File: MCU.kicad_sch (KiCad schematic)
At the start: 31 parts, among them J10 SWD, J11 UART, J12 I2C1, Q16 AO3401A, Q17 2N7002W, U12 STM32F030C8Tx

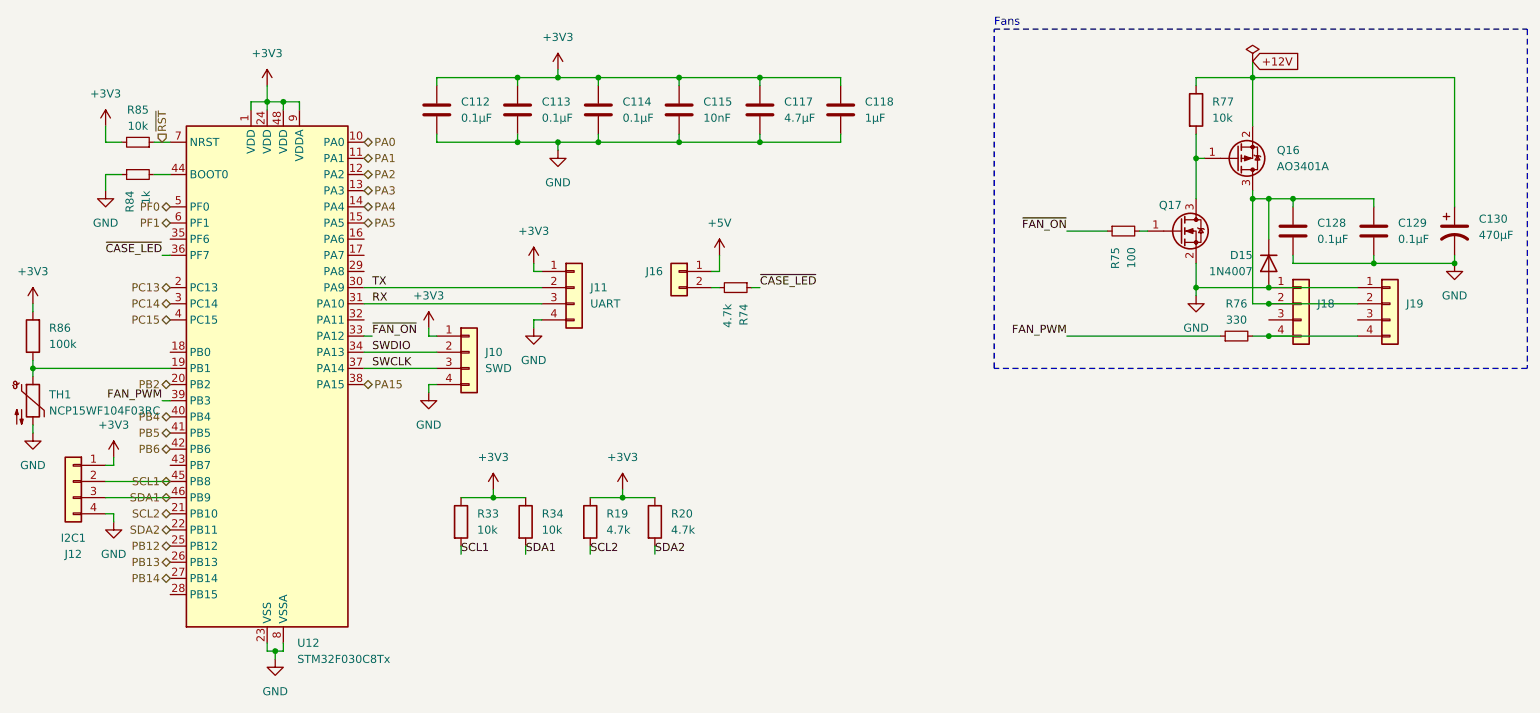
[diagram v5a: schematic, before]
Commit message: pcb: fixed fan capacitor and changed case led resistor value
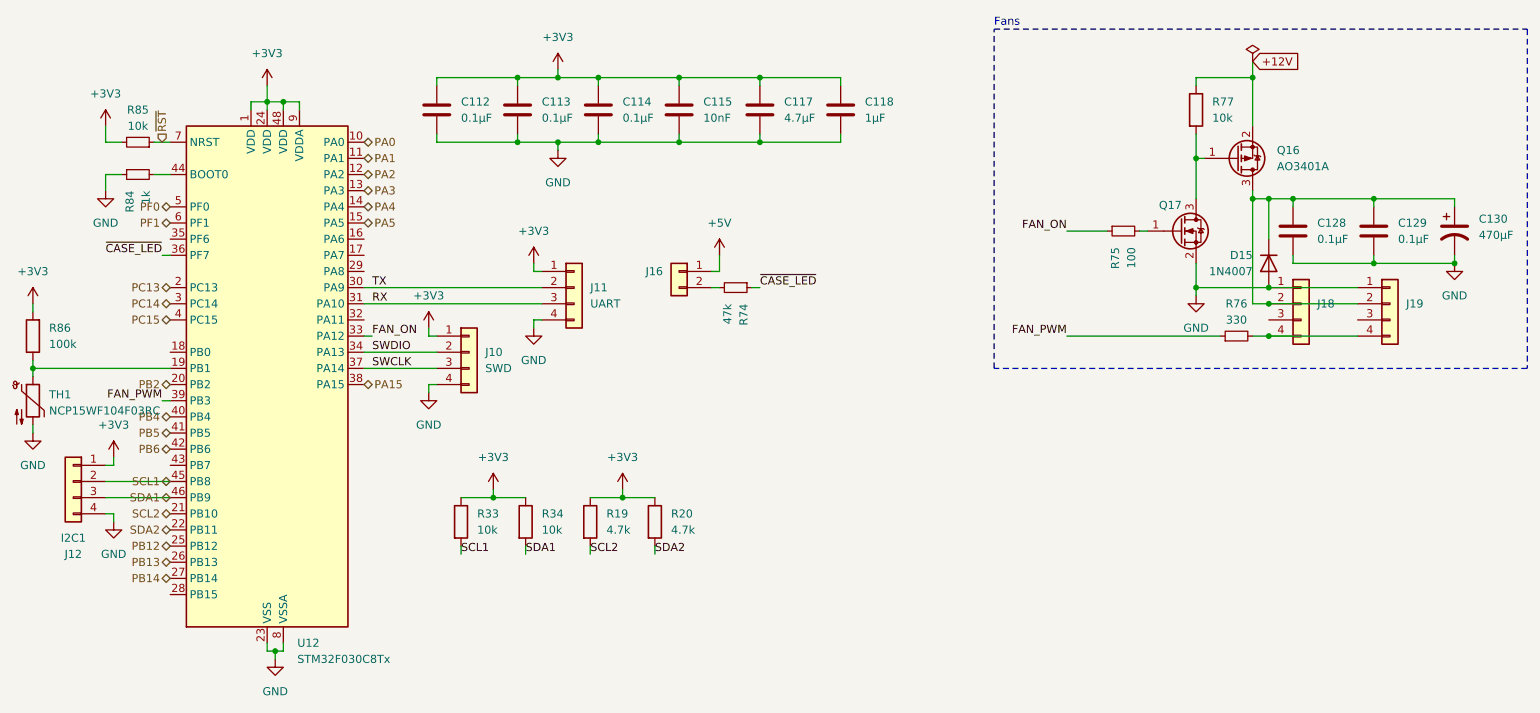
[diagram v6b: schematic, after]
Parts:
- R74: value 4.7k -> 47k; LCSC C25900 -> C25792; Part_Number 0402WGF4701TCE -> 0402WGF4702TCE
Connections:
- net +12V: no longer C130.1
- net at C128.1, C129.1, D15.1 (K)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: now also C130.1
- net ~{FAN_ON} renamed FAN_ON
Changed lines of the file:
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@@
 	)
 	(junction
+		(at 229.87 49.53)
+		(diameter 0)
+		(color 0 0 0 0)
+	)
+	(junction
 		(at 213.36 66.04)
 		(diameter 0)
@@
 	(wire
 		(pts
-			(xy 242.57 30.48) (xy 210.82 30.48)
+			(xy 30.48 45.72) (xy 30.48 48.26)
 		)
 		(stroke
@@
 	(wire
 		(pts
-			(xy 30.48 45.72) (xy 30.48 48.26)
+			(xy 229.87 49.53) (xy 229.87 50.8)
 		)
 		(stroke
@@
 	(wire
 		(pts
-			(xy 229.87 49.53) (xy 229.87 50.8)
+			(xy 86.36 104.14) (xy 86.36 105.41)
 		)
 		(stroke
@@
 	(wire
 		(pts
-			(xy 242.57 30.48) (xy 242.57 50.8)
+			(xy 95.25 30.48) (xy 101.6 30.48)
 		)
 		(stroke
@@
 	(wire
 		(pts
-			(xy 86.36 104.14) (xy 86.36 105.41)
+			(xy 30.48 91.44) (xy 31.75 91.44)
 		)
 		(stroke
@@
 	(wire
 		(pts
-			(xy 95.25 30.48) (xy 101.6 30.48)
+			(xy 120.65 40.64) (xy 120.65 39.37)
 		)
 		(stroke
@@
 	(wire
 		(pts
-			(xy 30.48 91.44) (xy 31.75 91.44)
+			(xy 127 63.5) (xy 125.73 63.5)
 		)
 		(stroke
@@
 	(wire
 		(pts
-			(xy 120.65 40.64) (xy 120.65 39.37)
+			(xy 71.12 71.12) (xy 72.39 71.12)
 		)
 		(stroke
@@
 	(wire
 		(pts
-			(xy 127 63.5) (xy 125.73 63.5)
+			(xy 229.87 49.53) (xy 242.57 49.53)
 		)
 		(stroke
@@
 	(wire
 		(pts
-			(xy 71.12 71.12) (xy 72.39 71.12)
+			(xy 217.17 58.42) (xy 217.17 59.69)
 		)
 		(stroke
@@
 	(wire
 		(pts
-			(xy 217.17 58.42) (xy 217.17 59.69)
+			(xy 181.61 71.12) (xy 205.74 71.12)
 		)
 		(stroke
@@
 	(wire
 		(pts
-			(xy 181.61 71.12) (xy 205.74 71.12)
+			(xy 242.57 49.53) (xy 242.57 50.8)
 		)
 		(stroke
@@
 		)
 	)
-	(label "~{FAN_ON}"
+	(label "FAN_ON"
 		(at 72.39 71.12 0)
 		(fields_autoplaced yes)
@@
 		)
 	)
-	(label "~{FAN_ON}"
+	(label "FAN_ON"
 		(at 181.61 54.61 180)
 		(fields_autoplaced yes)
@@
 			)
 		)
-		(property "Value" "4.7k"
+		(property "Value" "47k"
 			(at 128.2701 66.04 0)
 			(effects
@@
 			)
 		)
-		(property "Part_Number" "0402WGF4701TCE"
+		(property "Part_Number" "0402WGF4702TCE"
 			(at 129.54 63.5 0)
 			(effects
@@
 			)
 		)
-		(property "LCSC" "C25900"
+		(property "LCSC" "C25792"
 			(at 129.54 63.5 0)
 			(effects
